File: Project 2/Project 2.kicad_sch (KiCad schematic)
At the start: 50 parts, among them J1 Conn_01x05_Female, J2 Jack-DC, U1 ATmega2560-16A, U2 L7805

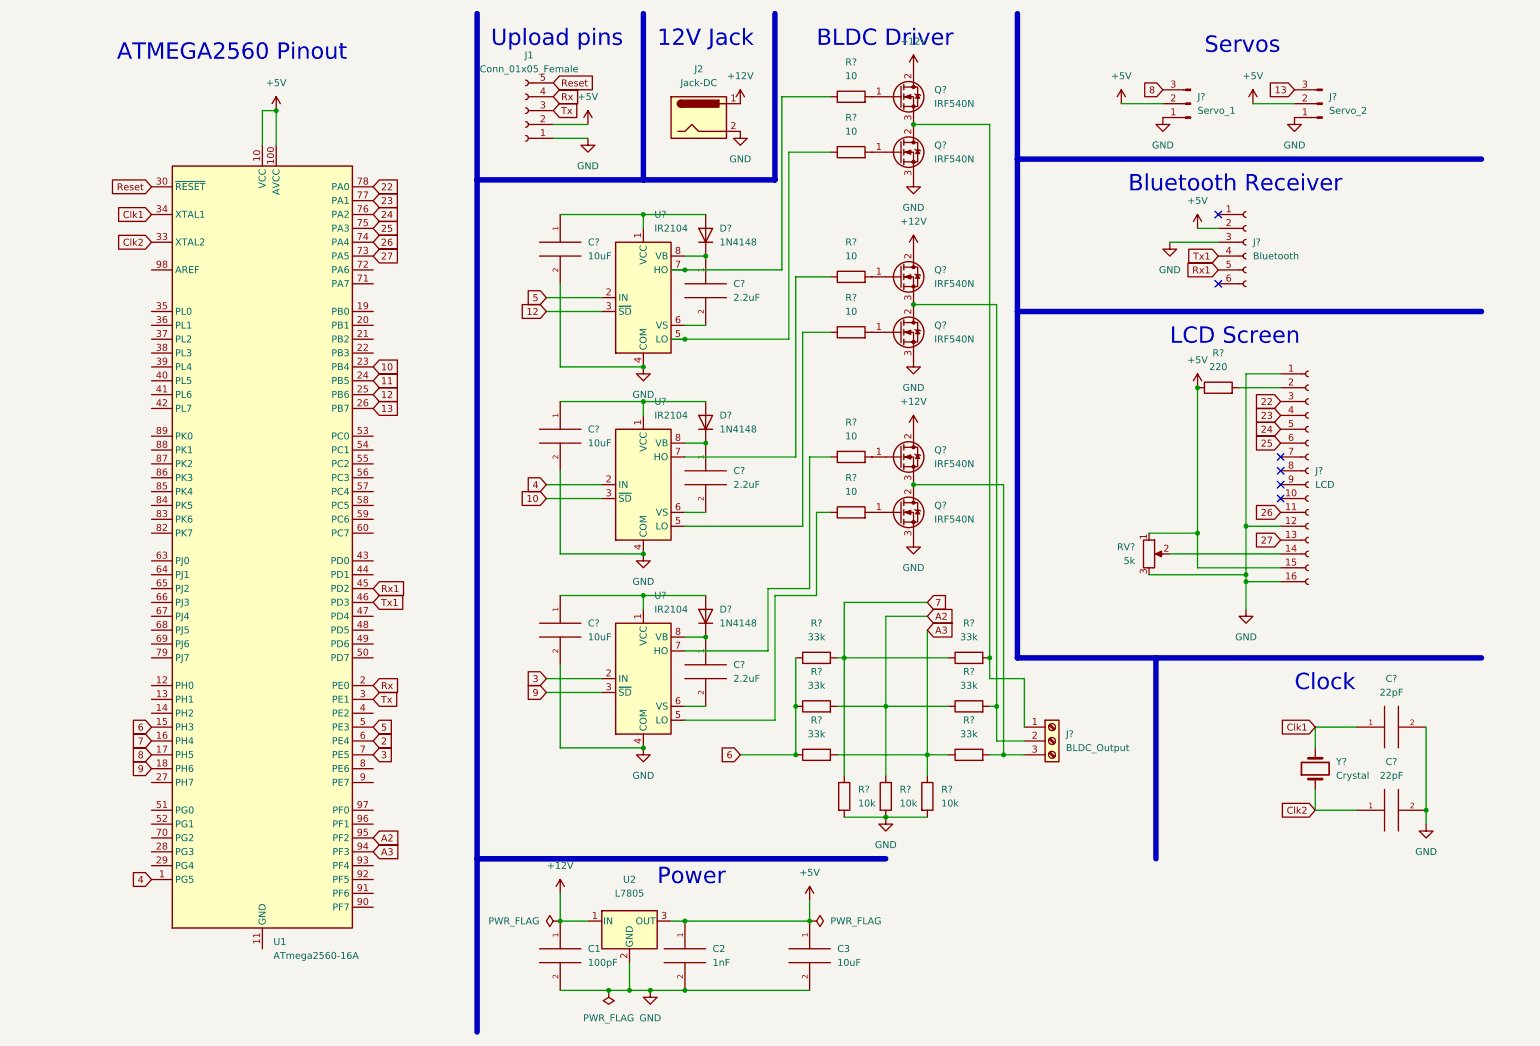
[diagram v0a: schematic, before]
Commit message: added ATMEDA2560 breakout board footprint
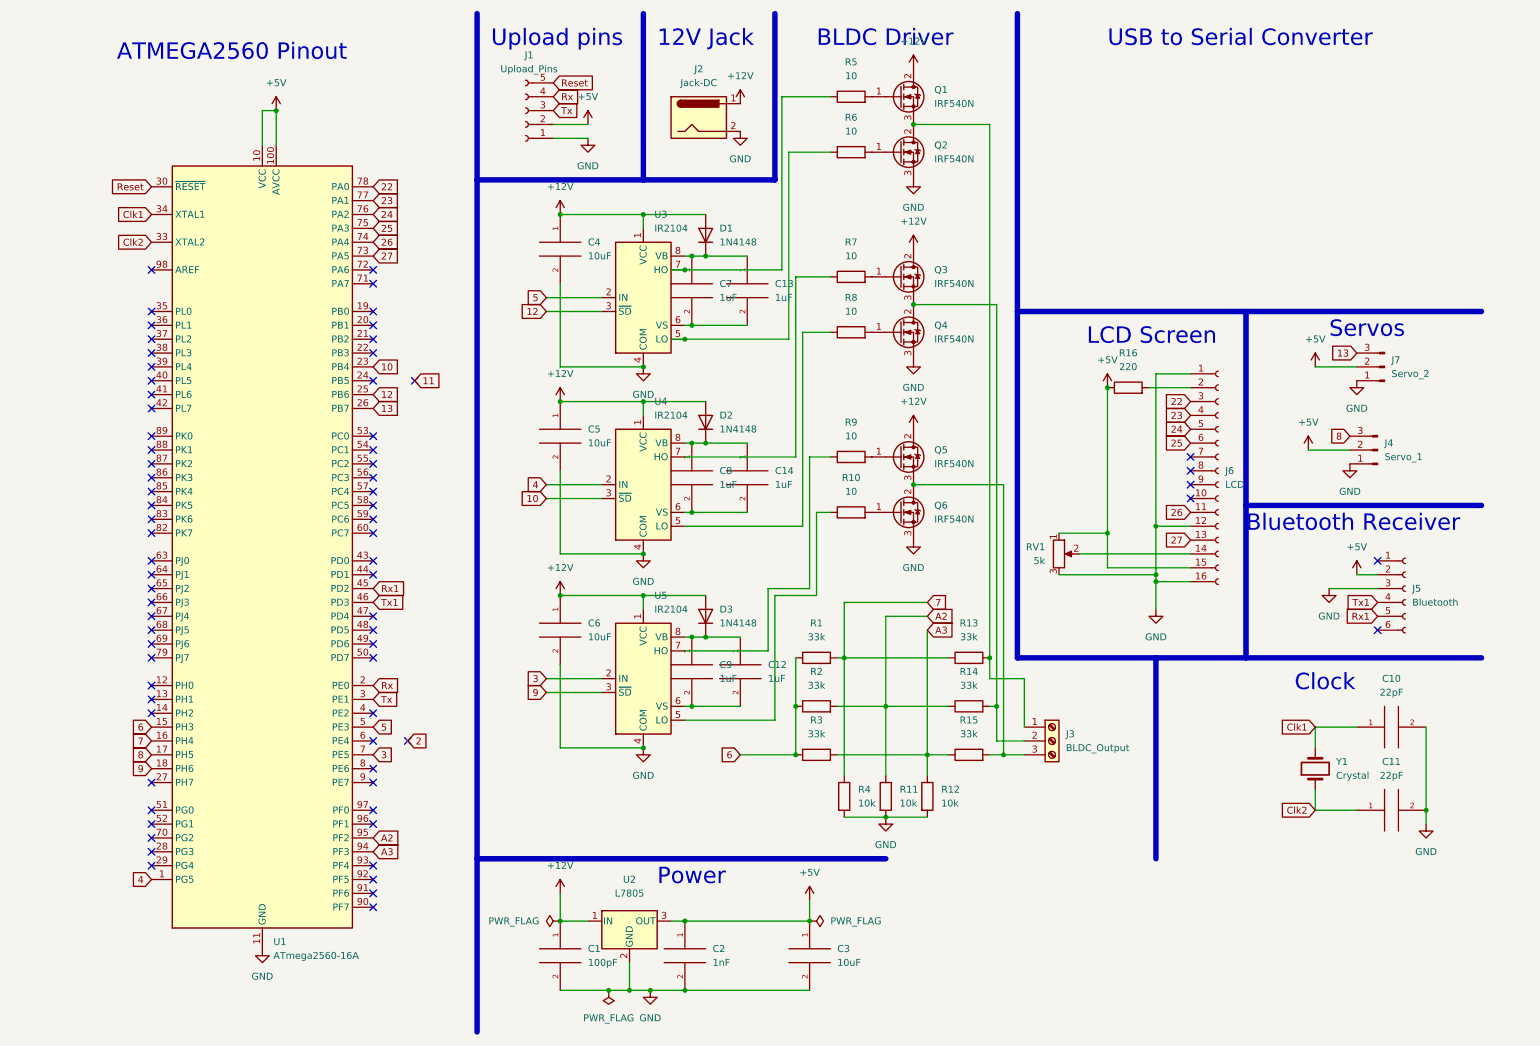
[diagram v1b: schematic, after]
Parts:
- added C12, C13, C14: 1uF, symbol pspice:CAP
- C7, C8, C9: renamed from C?; value 2.2uF -> 1uF
- J1: value Conn_01x05_Female -> Upload_Pins; footprint (none) -> Connector_PinSocket_2.54mm:PinSocket_1x05_P2.54mm_Vertical
- J4, J7: renamed from J?; footprint (none) -> Connector_PinHeader_2.54mm:PinHeader_1x03_P2.54mm_Vertical
- J5: renamed from J?; footprint (none) -> Connector_PinSocket_2.54mm:PinSocket_1x06_P2.54mm_Vertical
- J6: renamed from J?; footprint (none) -> Connector_PinSocket_2.54mm:PinSocket_1x16_P2.54mm_Vertical
- R1, R10, R11, R12, R13, R14, R15, R16, R2, R3, R4, R5, R6, R7, R8, R9: renamed from R?; footprint (none) -> Resistor_THT:R_Axial_DIN0207_L6.3mm_D2.5mm_P7.62mm_Horizontal
- U1: footprint Package_QFP:TQFP-100_14x14mm_P0.5mm -> custom:ATMEGA2560_breakout_Board_Socket
- U2: footprint (none) -> Package_TO_SOT_THT:TO-220-3_Vertical
- gave numbers to parts that had none: 20
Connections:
- net +12V: now also C4.1, C5.1, C6.1, D1.2 (A), D2.2 (A), D3.2 (A), U3.1 (VCC), U4.1 (VCC), U5.1 (VCC)
- net 11: no longer U1.24 (PB5)
- net 2: no longer U1.6 (PE4)
- net GND: now also U1.11 (GND), U1.32 (GND), U1.62 (GND), U1.81 (GND), U1.99 (GND)
- net at C9.1, D3.1 (K), U5.8 (VB): now also C12.1
- net at C9.2, U5.6 (VS): now also C12.2
- net at C7.2, U3.6 (VS): now also C13.2
- net at C7.1, D1.1 (K), U3.8 (VB): now also C13.1
- net at C8.1, D2.1 (K), U4.8 (VB): now also C14.1
- net at C8.2, U4.6 (VS): now also C14.2
- no-connect marks 6 -> 73
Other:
- note added: "USB to Serial Converter"
- moved on the sheet: C7, C8, C9, J4, J5, J6, J7, R16, RV1

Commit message: initial PCB design
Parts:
- removed J1: Upload_Pins, Connector_PinSocket_2.54mm:PinSocket_1x05_P2.54mm_Vertical, symbol Connector:Conn_01x05_Female
- added C15: 1uF, Capacitor_THT:C_Radial_D5.0mm_H11.0mm_P2.00mm, symbol pspice:CAP
- added C16: 1nF, Capacitor_THT:C_Disc_D3.0mm_W2.0mm_P2.50mm, symbol pspice:CAP
- added J1: USB_B, Connector_USB:USB_B_Lumberg_2411_02_Horizontal, symbol Connector:USB_B
- added R17: 10k, Resistor_THT:R_Axial_DIN0207_L6.3mm_D2.5mm_P7.62mm_Horizontal, symbol Device:R
- added R18: 4.7k, Resistor_THT:R_Axial_DIN0207_L6.3mm_D2.5mm_P7.62mm_Horizontal, symbol Device:R
- added R19, R20: 220, Resistor_THT:R_Axial_DIN0207_L6.3mm_D2.5mm_P7.62mm_Horizontal, symbol Device:R
- added SW1: Reset_Button, Button_Switch_THT:SW_PUSH_6mm_H4.3mm, symbol Switch:SW_Push
- added U6: mystery_uart_thing, Package_SO:SOP-16_3.9x9.9mm_P1.27mm, symbol Custom:mystery_uart_thing
- C1: value 100pF -> 1nF; footprint (none) -> Capacitor_THT:C_Disc_D3.0mm_W2.0mm_P2.50mm
- C10, C11: footprint (none) -> Capacitor_THT:C_Disc_D3.0mm_W2.0mm_P2.50mm
- C12, C13, C14, C3, C4, C5, C6, C7, C8, C9: footprint (none) -> Capacitor_THT:C_Radial_D5.0mm_H11.0mm_P2.00mm
- C2: value 1nF -> 100pF; footprint (none) -> Capacitor_THT:C_Disc_D3.0mm_W2.0mm_P2.50mm
- J2: footprint (none) -> Connector_BarrelJack:BarrelJack_GCT_DCJ200-10-A_Horizontal
- J3: footprint (none) -> TerminalBlock:TerminalBlock_Altech_AK300-3_P5.00mm
- J6: footprint Connector_PinSocket_2.54mm:PinSocket_1x16_P2.54mm_Vertical -> Display:WC1602A
- RV1: footprint (none) -> Potentiometer_THT:Potentiometer_Bourns_3386P_Vertical
- U3, U4, U5: footprint (none) -> Package_SO:SOIC-8_3.9x4.9mm_P1.27mm
- Y1: footprint (none) -> Crystal:Crystal_AT310_D3.0mm_L10.0mm_Vertical
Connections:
- net +5V: now also J6.2 (Pin_2), J1.1 (VBUS), R17.1, R18.2, U6.10 (5V), U6.14 (5V), U6.8 (5V); no longer J6.15 (Pin_15)
- net 22: now also J6.14 (Pin_14); no longer J6.3 (Pin_3)
- net 23: now also J6.13 (Pin_13); no longer J6.4 (Pin_4)
- net 24: now also J6.12 (Pin_12); no longer J6.5 (Pin_5)
- net 25: now also J6.11 (Pin_11); no longer J6.6 (Pin_6)
- net 26: now also J6.6 (Pin_6); no longer J6.11 (Pin_11)
- net 27: now also J6.4 (Pin_4); no longer J6.13 (Pin_13)
- net GND: now also J6.5 (Pin_5), C15.2, J1.4 (GND), SW1.2, U6.7 (GND), U6.9 (GND); no longer J6.12 (Pin_12)
- net Reset: now also C16.2, R17.2, SW1.1
- net Rx: now also R19.2
- net Tx: now also R20.2
- net at R16.2: now also J6.15 (Pin_15); no longer J6.2 (Pin_2)
- net at RV1.2: now also J6.3 (Pin_3); no longer J6.14 (Pin_14)
- new net: R19.1, U6.11 (Tx)
- new net: R18.1, U6.1 (group1), U6.16 (group4), U6.2 (group2), U6.3 (Group3)
- new net: C15.1, U6.6 (capGND)
- new net: C16.1, U6.12 (RESET)
- new net: R20.1, U6.15 (Rx)
- new net D+: J1.3 (D+), U6.4 (D+)
- new net D-: J1.2 (D-), U6.5 (D-)
- no-connect marks 73 -> 75
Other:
- note added: "USB Port"
- note removed: "Upload pins"
